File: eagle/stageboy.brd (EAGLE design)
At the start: 120 x 75 mm, 35 parts, among them IC1 MEGA8-P, IC2 7805TV, Q1 16MHz, X1 MIDI IN, X2 MIDI OUT, X6 GBIO

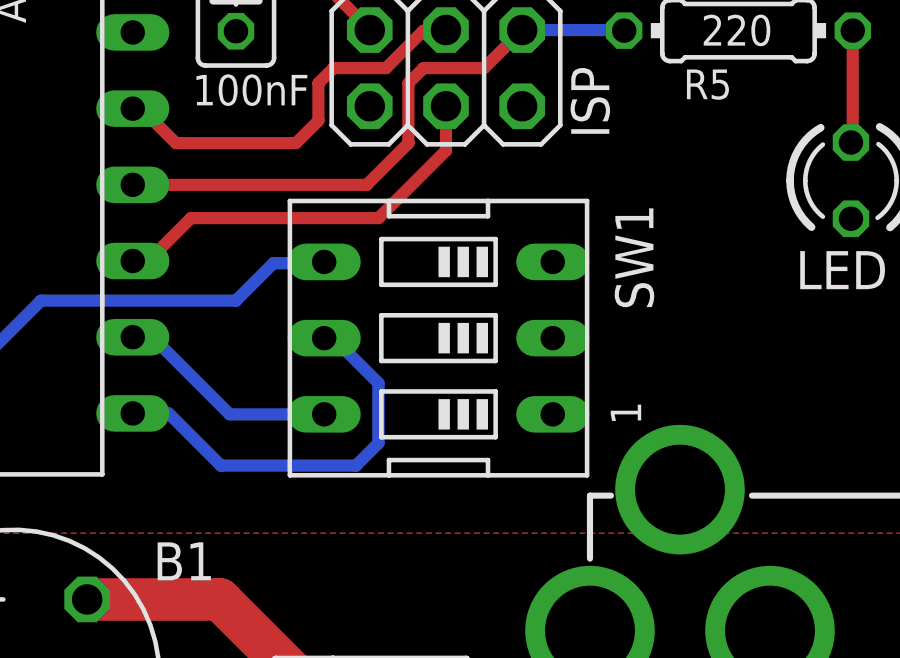
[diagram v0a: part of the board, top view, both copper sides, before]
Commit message: Moved the DIP switch around a bit
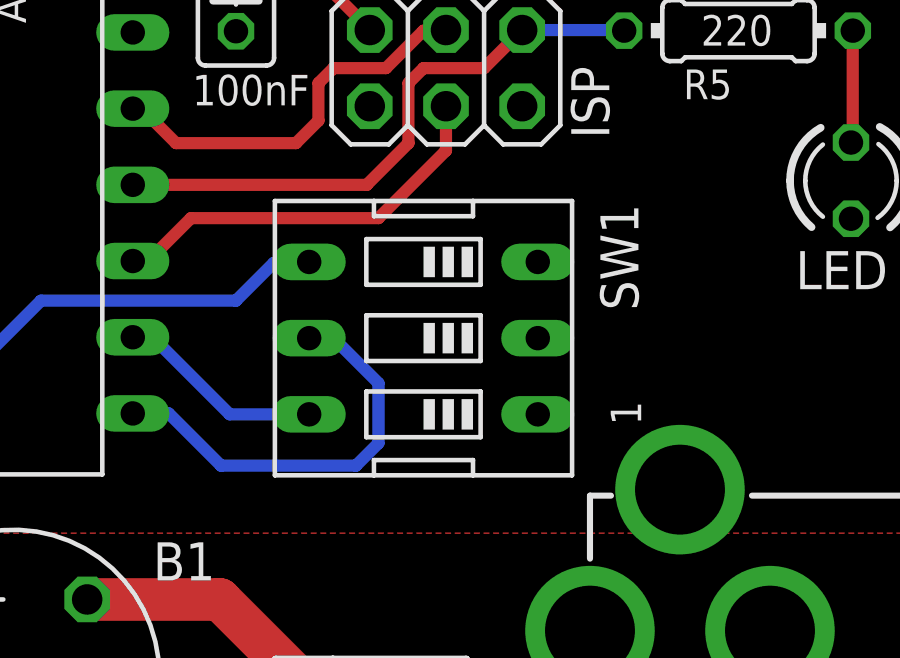
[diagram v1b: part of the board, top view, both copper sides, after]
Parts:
- moved SW1 0.50 mm to (100.8, 19.2)
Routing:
- net N$6: track 7.44 -> 6.94 mm
- net N$5: track 13.7 -> 14.2 mm
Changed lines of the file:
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@@
 </element>
 <element name="U$1" library="EDCOR" package="PCW-12PIN" value="EDCOR-PC600/600" x="50.25" y="48"/>
-<element name="SW1" library="special" package="EDG-03" value="" x="101.25" y="19.25" smashed="yes" rot="R90">
-<attribute name="VALUE" x="107.854" y="14.678" size="1.27" layer="27" ratio="10" rot="R90"/>
-<attribute name="NAME" x="108.416" y="20.178" size="1.27" layer="25" ratio="10" rot="R90"/>
+<element name="SW1" library="special" package="EDG-03" value="" x="100.75" y="19.25" smashed="yes" rot="R90">
+<attribute name="VALUE" x="107.354" y="14.678" size="1.27" layer="27" ratio="10" rot="R90"/>
+<attribute name="NAME" x="107.916" y="20.178" size="1.27" layer="25" ratio="10" rot="R90"/>
 </element>
 <element name="LED" library="led" package="LED3MM" value="" x="115" y="24.5" locked="yes" smashed="yes" rot="R270">
@@
 <wire x1="88" y1="20.5" x2="94.5" y2="20.5" width="0.4064" layer="16"/>
 <wire x1="94.5" y1="20.5" x2="95.75" y2="21.75" width="0.4064" layer="16"/>
-<wire x1="97.15" y1="21.75" x2="95.75" y2="21.75" width="0.4064" layer="16"/>
-<wire x1="97.15" y1="21.75" x2="97.44" y2="21.79" width="0" layer="19" extent="16-16"/>
+<wire x1="95.75" y1="21.75" x2="96.9" y2="21.75" width="0.4064" layer="16"/>
+<wire x1="96.9" y1="21.75" x2="96.94" y2="21.79" width="0.4064" layer="16"/>
 </signal>
 <signal name="N$5">
@@
 <wire x1="99.25" y1="15.75" x2="99.25" y2="17.75" width="0.4064" layer="16"/>
 <wire x1="99.25" y1="17.75" x2="97.75" y2="19.25" width="0.4064" layer="16"/>
-<wire x1="97.75" y1="19.25" x2="97.44" y2="19.25" width="0.4064" layer="16"/>
+<wire x1="97.75" y1="19.25" x2="96.94" y2="19.25" width="0.4064" layer="16"/>
 </signal>
 <signal name="N$6">
@@
 <wire x1="91.06" y1="19.28" x2="91.72" y2="19.28" width="0.4064" layer="16"/>
 <wire x1="91.72" y1="19.28" x2="94.29" y2="16.71" width="0.4064" layer="16"/>
-<wire x1="97.44" y1="16.71" x2="94.29" y2="16.71" width="0.4064" layer="16"/>
+<wire x1="96.94" y1="16.71" x2="94.29" y2="16.71" width="0.4064" layer="16"/>
 </signal>
 </signals>

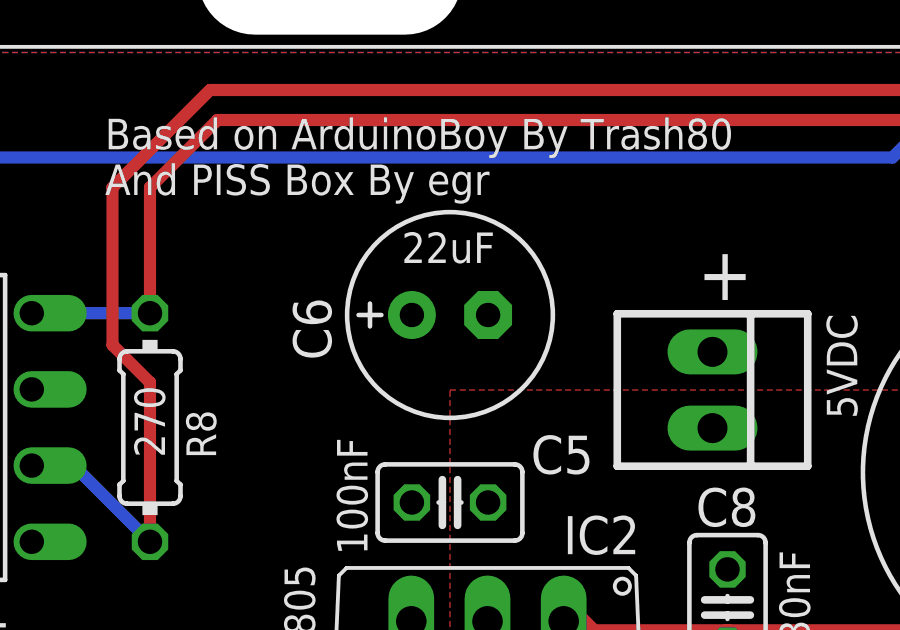
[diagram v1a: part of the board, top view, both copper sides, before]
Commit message: Added Bill of Materials
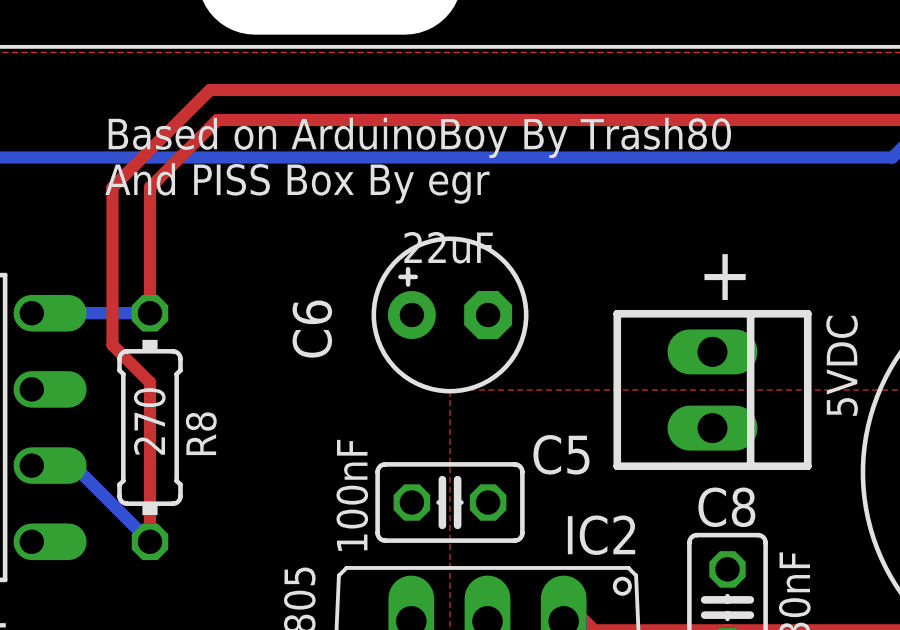
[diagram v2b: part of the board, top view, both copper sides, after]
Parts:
- C6: device resistor:E2,5-7 -> resistor:E2,5-5
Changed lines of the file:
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@@
 <attribute name="VALUE" x="17.825" y="16.54" size="1.27" layer="27" rot="R270"/>
 </element>
-<element name="C6" library="resistor" package="E2,5-7" value="22uF" x="54.25" y="15.25" smashed="yes">
+<element name="C6" library="resistor" package="E2,5-5" value="22uF" x="54.25" y="15.25" smashed="yes">
 <attribute name="NAME" x="49.024" y="15.833" size="1.27" layer="25" ratio="10" rot="R270"/>
 <attribute name="VALUE" x="56.917" y="12.583" size="1.27" layer="27" ratio="10"/>
